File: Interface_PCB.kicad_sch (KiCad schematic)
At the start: 48 parts, among them IC1 STM32L412RBT6P, J1 Conn_01x04, J2 Conn_01x04, J3 Conn_01x04, J4 Conn_01x04, J5 AVR-JTAG-10, J6 Micro_SD_Card, J7 USB_B, J9 Conn_01x02_Male, U1 AMS1117-3.3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

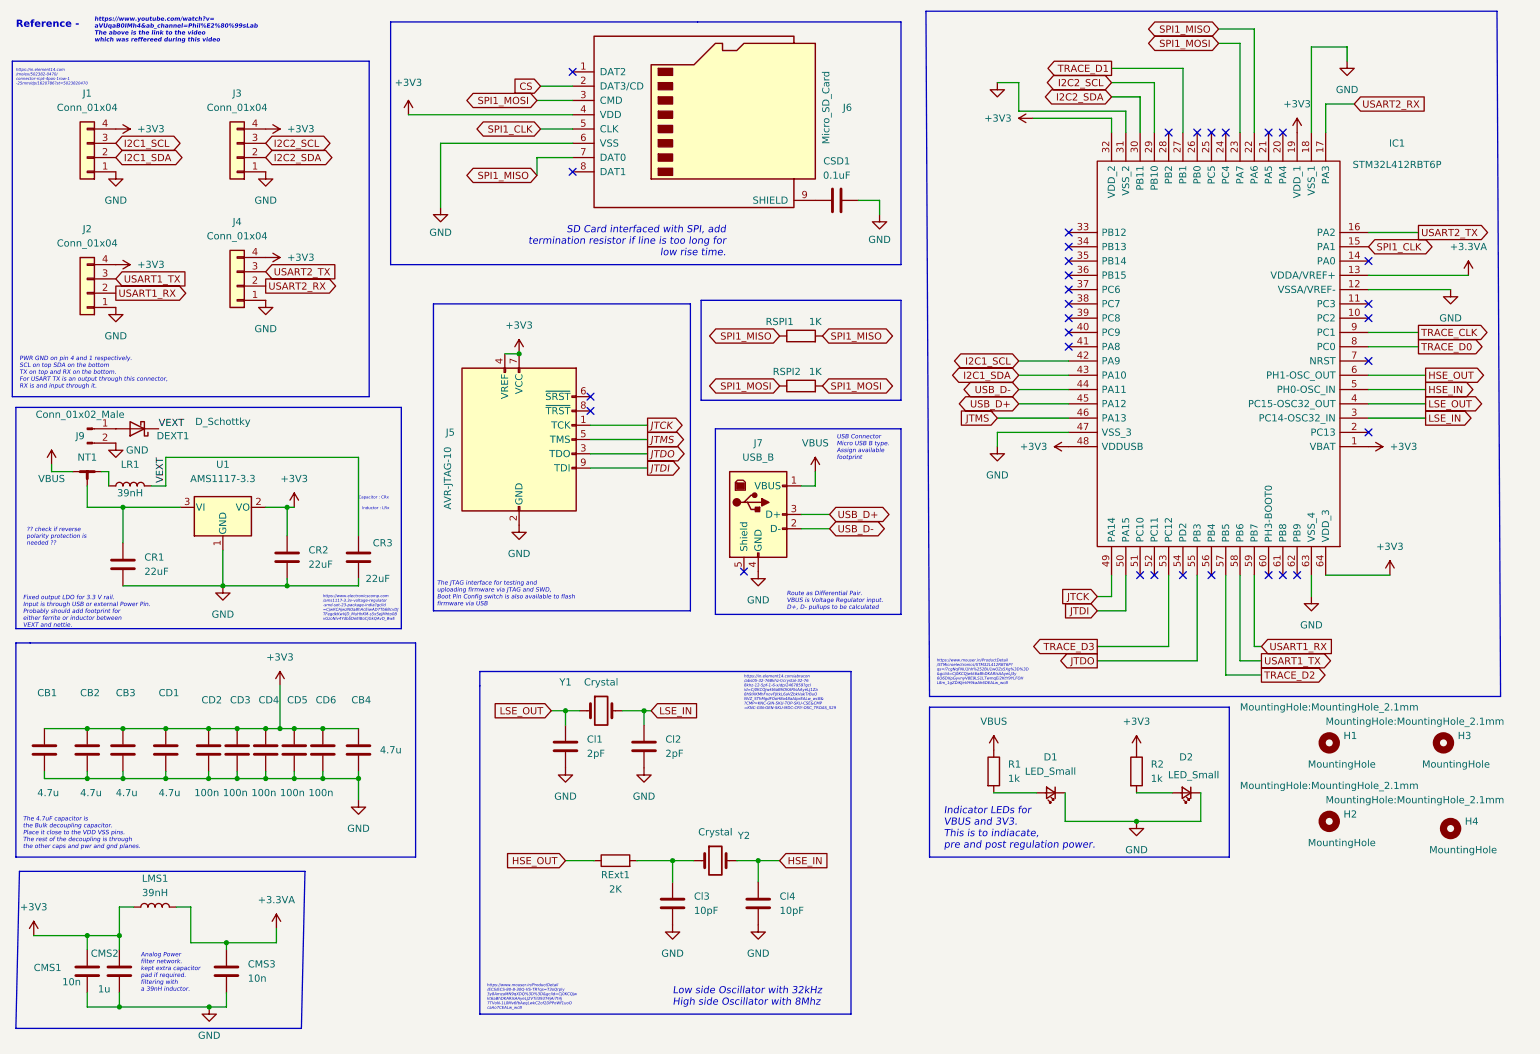
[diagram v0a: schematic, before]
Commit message: Updated inductor and USB according to manufacturer
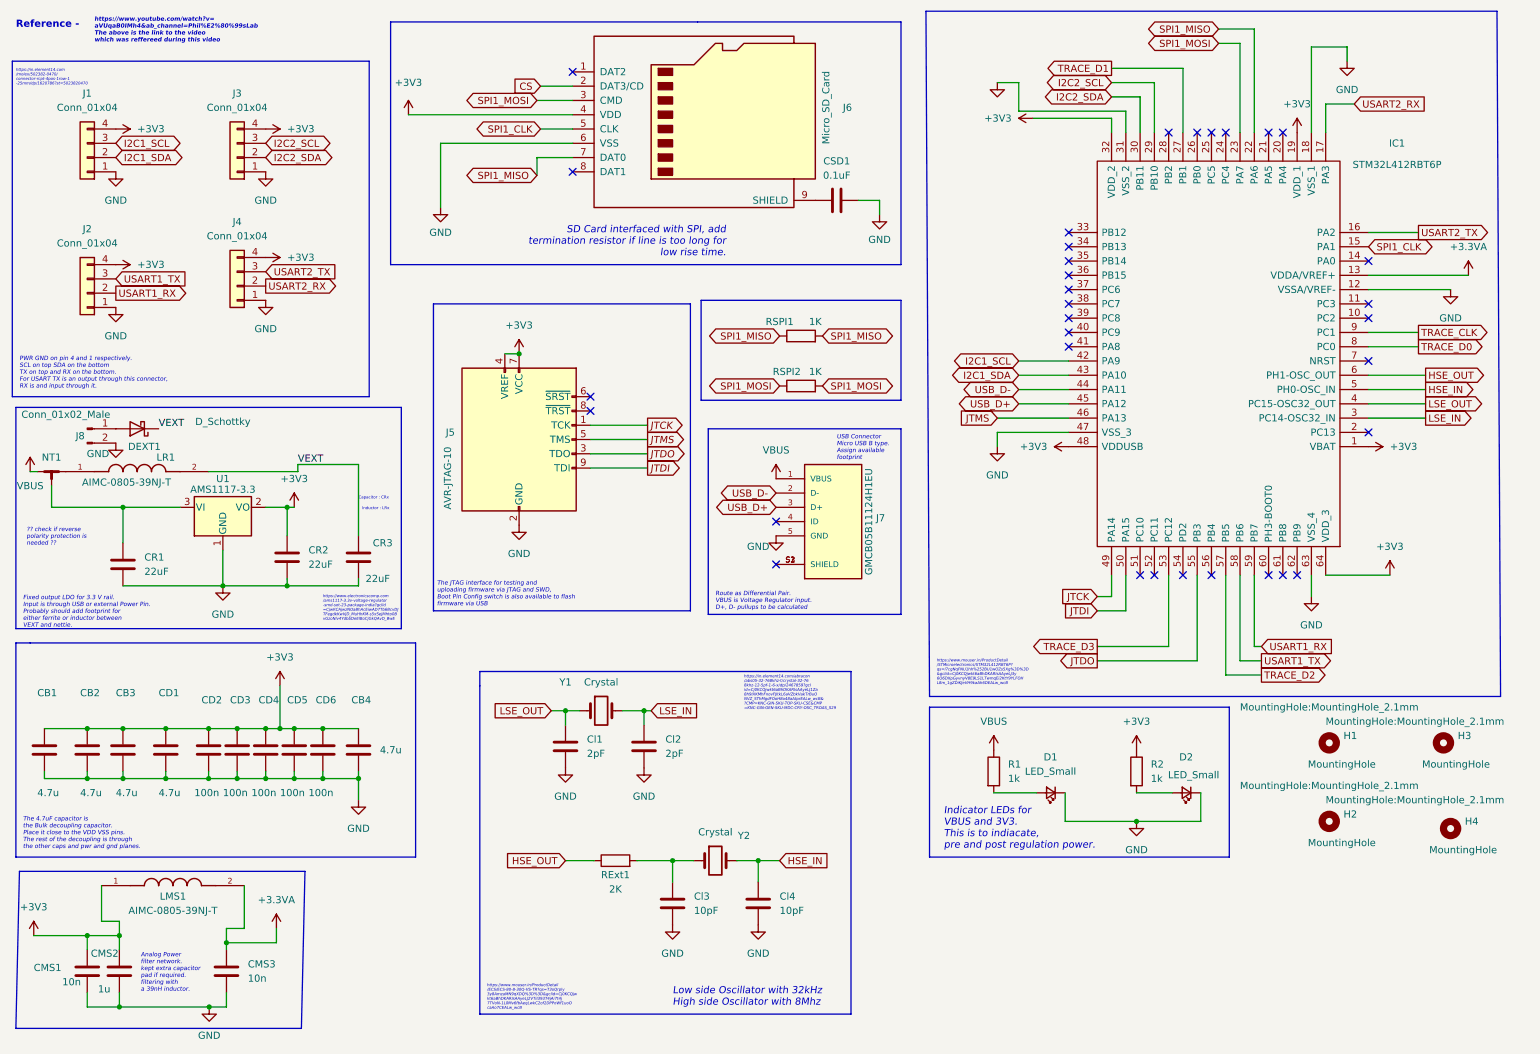
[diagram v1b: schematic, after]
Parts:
- removed J7: USB_B, SamacSys_Parts:GMCB05B11124H1EU, symbol Connector:USB_B
- removed LMS1, LR1: 39nH, Inductor_SMD:L_0805_2012Metric, symbol Device:L
- added J7: GMCB05B11124H1EU, GMCB05B11124H1EU (1):AMPHENOL_GMCB05B11124H1EU, symbol GMCB05B11124H1EU:GMCB05B11124H1EU
- added LMS1, LR1: AIMC-0805-39NJ-T, INDC2012X105N, symbol AIMC-0805-39NJ-T:AIMC-0805-39NJ-T
- renumbered J9 to J8
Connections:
- net +3.3VA: now also LMS1.2
- net +3V3: now also LMS1.1
- net GND: now also J7.5 (GND)
- net USB_D+: now also J7.3 (D+)
- net USB_D-: now also J7.2 (D-)
- net VBUS: now also J7.1 (VBUS)
- net VEXT: now also LR1.2
- net at NT1.2: now also LR1.1
- new net: J7.S1 (SHIELD), J7.S2 (SHIELD), J7.S3 (SHIELD)
- no-connect marks 32 -> 33
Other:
- moved on the sheet: NT1
